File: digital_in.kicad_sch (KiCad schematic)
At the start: 18 parts, among them U27 AM26LV32E

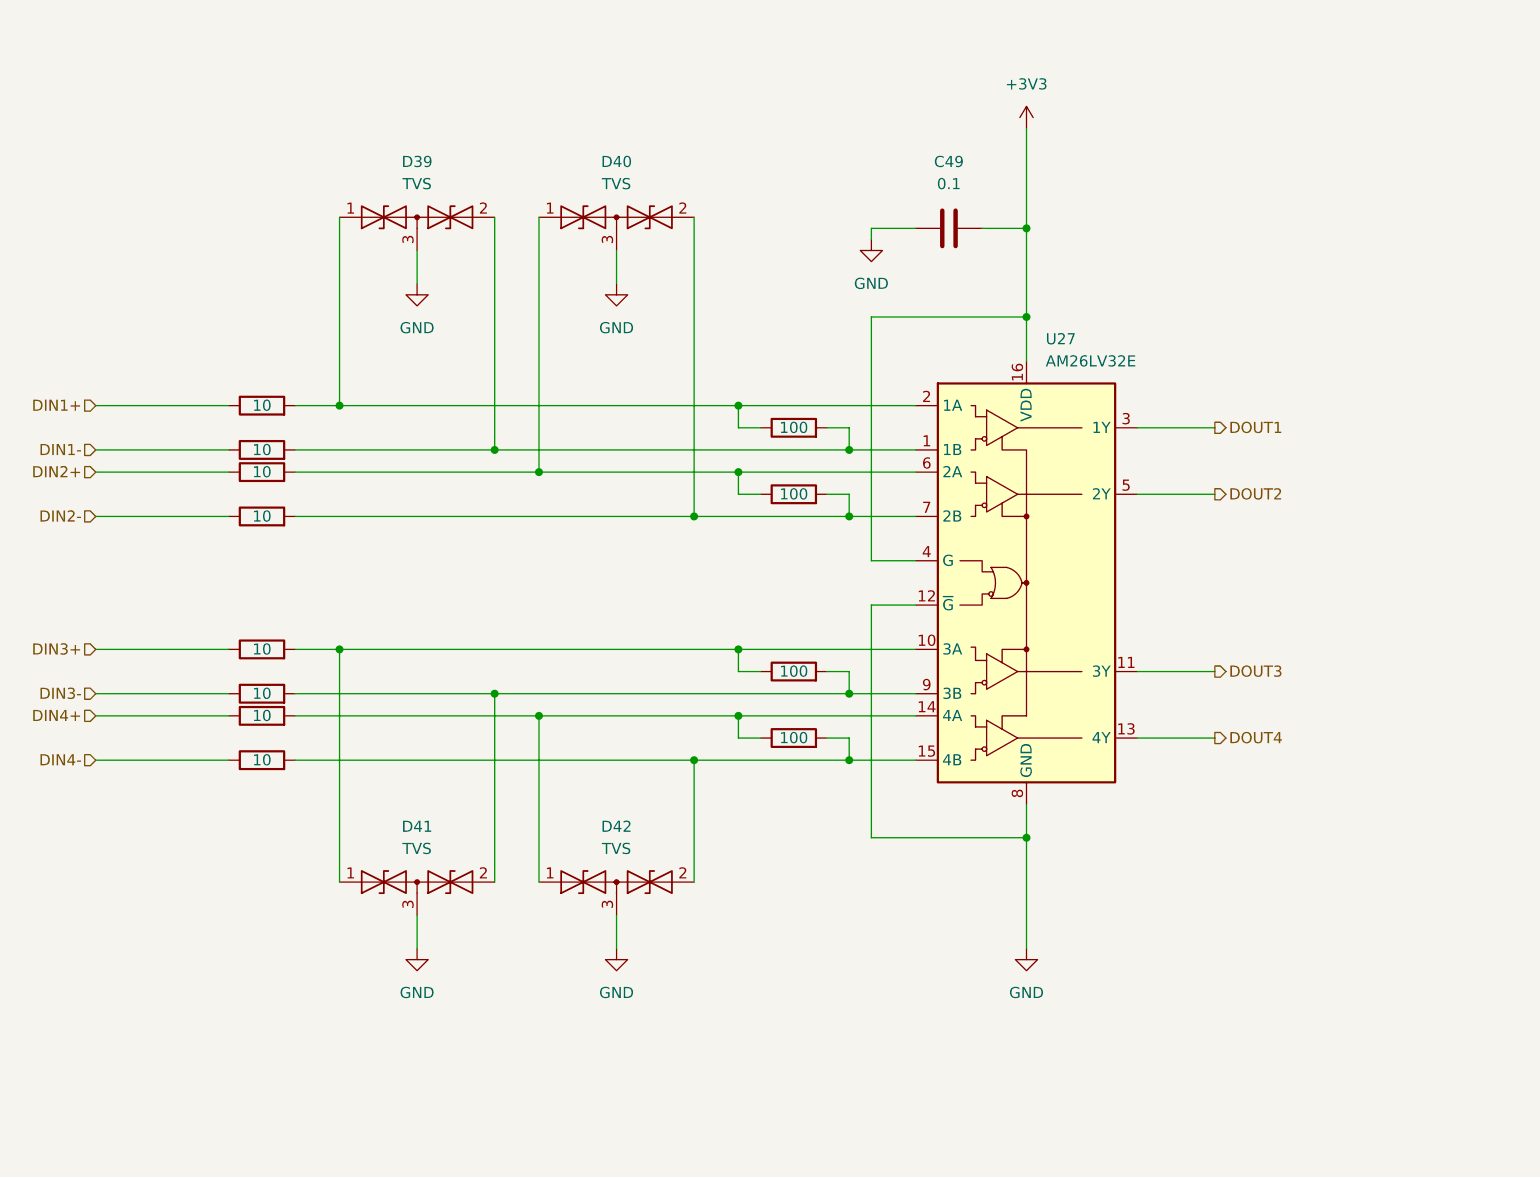
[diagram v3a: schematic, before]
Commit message: Adjusted components in I/O circuits
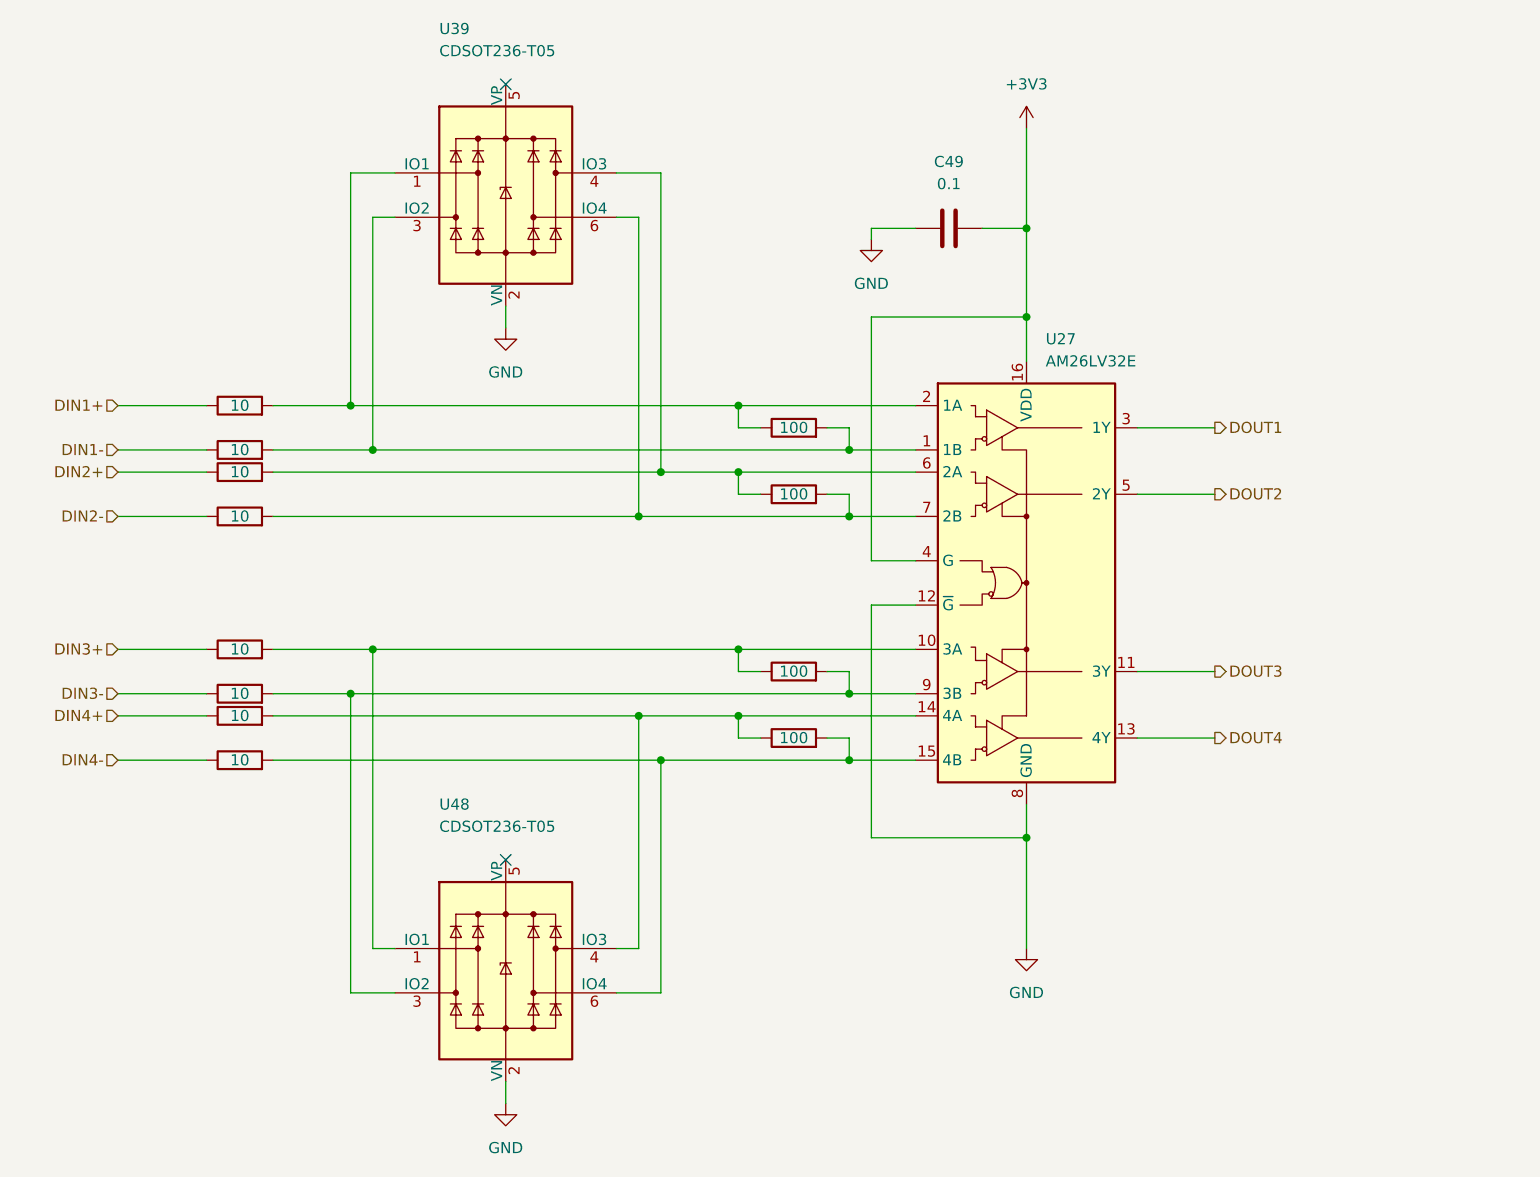
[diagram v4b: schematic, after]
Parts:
- removed D39, D40, D41, D42: TVS, Package_TO_SOT_SMD:SOT-23, symbol Diode:SM712_SOT23
- added U39, U48: CDSOT236-T05, Package_TO_SOT_SMD:SOT-23-6, symbol Power_Protection:CDSOT236-0504C
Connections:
- net GND: now also U39.2 (VN), U48.2 (VN)
- net at R153.2, R154.2, U27.15 (4B): now also U48.6 (IO4)
- net at R149.2, R150.1, U27.10 (3A): now also U48.1 (IO1)
- net at R150.2, R151.2, U27.9 (3B): now also U48.3 (IO2)
- net at R147.2, R148.2, U27.7 (2B): now also U39.6 (IO4)
- net at R152.2, R153.1, U27.14 (4A): now also U48.4 (IO3)
- net at R144.2, R145.2, U27.1 (1B): now also U39.3 (IO2)
- net at R143.2, R144.1, U27.2 (1A): now also U39.1 (IO1)
- net at R146.2, R147.1, U27.6 (2A): now also U39.4 (IO3)
- no-connect marks 0 -> 2

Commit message: Assigned proper footprints for all components
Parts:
- C49: value 0.1 -> 100n; footprint (none) -> Capacitor_SMD:C_0603_1608Metric_Pad1.08x0.95mm_HandSolder
- R143, R144, R145, R146, R147, R148, R149, R150, R151, R152, R153, R154: footprint (none) -> Resistor_SMD:R_0603_1608Metric_Pad0.98x0.95mm_HandSolder
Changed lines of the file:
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@@
       (effects (font (size 1.27 1.27)))
     )
-    (property "Footprint" "" (at 102.87 119.888 90)
+    (property "Footprint" "Resistor_SMD:R_0603_1608Metric_Pad0.98x0.95mm_HandSolder" (at 102.87 119.888 90)
       (effects (font (size 1.27 1.27)) hide)
     )
@@
       (effects (font (size 1.27 1.27)))
     )
-    (property "Value" "0.1" (at 184.15 52.07 90)
-      (effects (font (size 1.27 1.27)))
-    )
-    (property "Footprint" "" (at 187.96 56.1848 0)
+    (property "Value" "100n" (at 184.15 52.07 90)
+      (effects (font (size 1.27 1.27)))
+    )
+    (property "Footprint" "Capacitor_SMD:C_0603_1608Metric_Pad1.08x0.95mm_HandSolder" (at 187.96 56.1848 0)
       (effects (font (size 1.27 1.27)) hide)
     )
@@
       (effects (font (size 1.27 1.27)))
     )
-    (property "Footprint" "" (at 102.87 107.188 90)
+    (property "Footprint" "Resistor_SMD:R_0603_1608Metric_Pad0.98x0.95mm_HandSolder" (at 102.87 107.188 90)
       (effects (font (size 1.27 1.27)) hide)
     )
@@
       (effects (font (size 1.27 1.27)))
     )
-    (property "Footprint" "" (at 102.87 112.268 90)
+    (property "Footprint" "Resistor_SMD:R_0603_1608Metric_Pad0.98x0.95mm_HandSolder" (at 102.87 112.268 90)
       (effects (font (size 1.27 1.27)) hide)
     )
@@
       (effects (font (size 1.27 1.27)))
     )
-    (property "Footprint" "" (at 102.87 91.948 90)
+    (property "Footprint" "Resistor_SMD:R_0603_1608Metric_Pad0.98x0.95mm_HandSolder" (at 102.87 91.948 90)
       (effects (font (size 1.27 1.27)) hide)
     )
@@
       (effects (font (size 1.27 1.27)))
     )
-    (property "Footprint" "" (at 102.87 114.808 90)
+    (property "Footprint" "Resistor_SMD:R_0603_1608Metric_Pad0.98x0.95mm_HandSolder" (at 102.87 114.808 90)
       (effects (font (size 1.27 1.27)) hide)
     )
@@
       (effects (font (size 1.27 1.27)))
     )
-    (property "Footprint" "" (at 166.37 109.728 90)
+    (property "Footprint" "Resistor_SMD:R_0603_1608Metric_Pad0.98x0.95mm_HandSolder" (at 166.37 109.728 90)
       (effects (font (size 1.27 1.27)) hide)
     )
@@
       (effects (font (size 1.27 1.27)))
     )
-    (property "Footprint" "" (at 166.37 89.408 90)
+    (property "Footprint" "Resistor_SMD:R_0603_1608Metric_Pad0.98x0.95mm_HandSolder" (at 166.37 89.408 90)
       (effects (font (size 1.27 1.27)) hide)
     )
@@
       (effects (font (size 1.27 1.27)))
     )
-    (property "Footprint" "" (at 166.37 117.348 90)
+    (property "Footprint" "Resistor_SMD:R_0603_1608Metric_Pad0.98x0.95mm_HandSolder" (at 166.37 117.348 90)
       (effects (font (size 1.27 1.27)) hide)
     )
@@
       (effects (font (size 1.27 1.27)))
     )
-    (property "Footprint" "" (at 102.87 86.868 90)
+    (property "Footprint" "Resistor_SMD:R_0603_1608Metric_Pad0.98x0.95mm_HandSolder" (at 102.87 86.868 90)
       (effects (font (size 1.27 1.27)) hide)
     )
@@
       (effects (font (size 1.27 1.27)))
     )
-    (property "Footprint" "" (at 166.37 81.788 90)
+    (property "Footprint" "Resistor_SMD:R_0603_1608Metric_Pad0.98x0.95mm_HandSolder" (at 166.37 81.788 90)
       (effects (font (size 1.27 1.27)) hide)
     )
@@
       (effects (font (size 1.27 1.27)))
     )
-    (property "Footprint" "" (at 102.87 79.248 90)
+    (property "Footprint" "Resistor_SMD:R_0603_1608Metric_Pad0.98x0.95mm_HandSolder" (at 102.87 79.248 90)
       (effects (font (size 1.27 1.27)) hide)
     )
@@
       (effects (font (size 1.27 1.27)))
     )
-    (property "Footprint" "" (at 102.87 84.328 90)
-      (effects (font (size 1.27 1.27)) hide)
-    )
+    (property "Footprint" "Resistor_SMD:R_0603_1608Metric_Pad0.98x0.95mm_HandSolder" (at 102.87 84.328 90)
+      (effects (font (size 1.27 1.27)) hide)
+    )

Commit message: Updated boards hierarchy
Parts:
- renumbered C49 to C1, R143 to R1, R152 to R10, R153 to R11, R154 to R12, R144 to R2, R145 to R3, R146 to R4, R147 to R5, R148 to R6, R149 to R7, R150 to R8, R151 to R9, U39 to U1, U27 to U20, U48 to U21

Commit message: Finished annotation
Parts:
- renumbered C1 to C1401, R1 to R1401, R2 to R1402, R3 to R1403, R4 to R1404, R5 to R1405, R6 to R1406, R7 to R1407, R8 to R1408, R9 to R1409, R10 to R1410, R11 to R1411, R12 to R1412, U1 to U1401, U20 to U1402, U21 to U1403
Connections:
- net DOUT1 renamed DIN1
- net DOUT2 renamed DIN2
- net DOUT3 renamed DIN3
- net DOUT4 renamed DIN4

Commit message: Fixed ERC errors and warnings
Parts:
- added R1103, R1105, R1108, R1110, R1113, R1115, R1118, R1120: 0, Resistor_SMD:R_0603_1608Metric_Pad0.98x0.95mm_HandSolder, symbol Device:R
- renumbered R1403 to R1404, R1404 to R1406, R1405 to R1407, R1406 to R1409, R1407 to R1411, R1408 to R1412, R1409 to R1414, R1410 to R1416, R1411 to R1417, R1412 to R1419
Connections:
- net DIN1: now also R1103.2; no longer U1402.3 (1Y)
- net DIN2: now also R1108.2; no longer U1402.5 (2Y)
- net DIN3: now also R1113.2; no longer U1402.11 (3Y)
- net DIN4: now also R1118.2; no longer U1402.13 (4Y)
- net at R1417.2, R1419.2, U1403.6 (IO4): now also R1120.1; no longer U1402.15 (4B)
- net at R1412.2, R1414.2, U1403.3 (IO2): now also R1115.1; no longer U1402.9 (3B)
- net at R1407.2, R1409.2, U1401.6 (IO4): now also R1110.1; no longer U1402.7 (2B)
- net at R1402.2, R1404.2, U1401.3 (IO2): now also R1105.1; no longer U1402.1 (1B)
- new net: R1118.1, U1402.13 (4Y)
- new net: R1105.2, U1402.1 (1B)
- new net: R1113.1, U1402.11 (3Y)
- new net: R1120.2, U1402.15 (4B)
- new net: R1103.1, U1402.3 (1Y)
- new net: R1108.1, U1402.5 (2Y)
- new net: R1110.2, U1402.7 (2B)
- new net: R1115.2, U1402.9 (3B)
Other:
- moved on the sheet: C1401, U1402
